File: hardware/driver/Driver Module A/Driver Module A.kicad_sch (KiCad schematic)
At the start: 22 parts, among them J1 Conn_01x02_Pin, J2 Conn_01x02_Pin, J3 Conn_01x01_Pin, J4 Conn_01x02_Pin

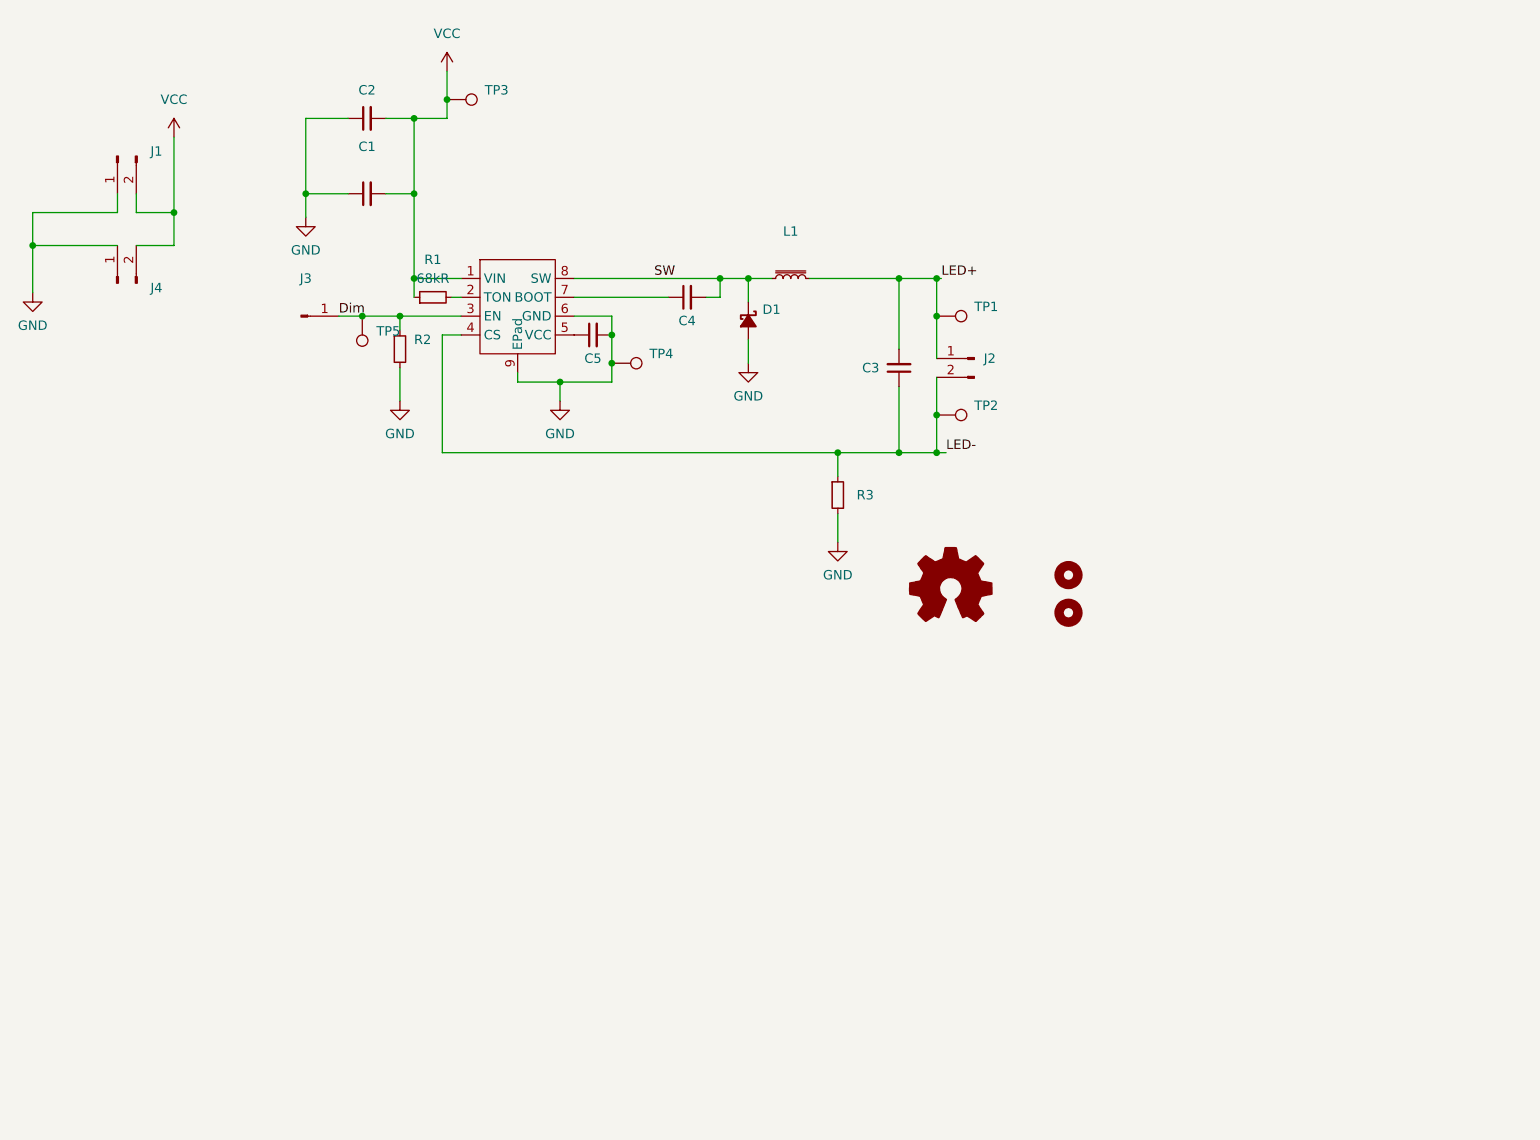
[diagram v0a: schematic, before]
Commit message: Minor silkscreen improvements on the driver module A
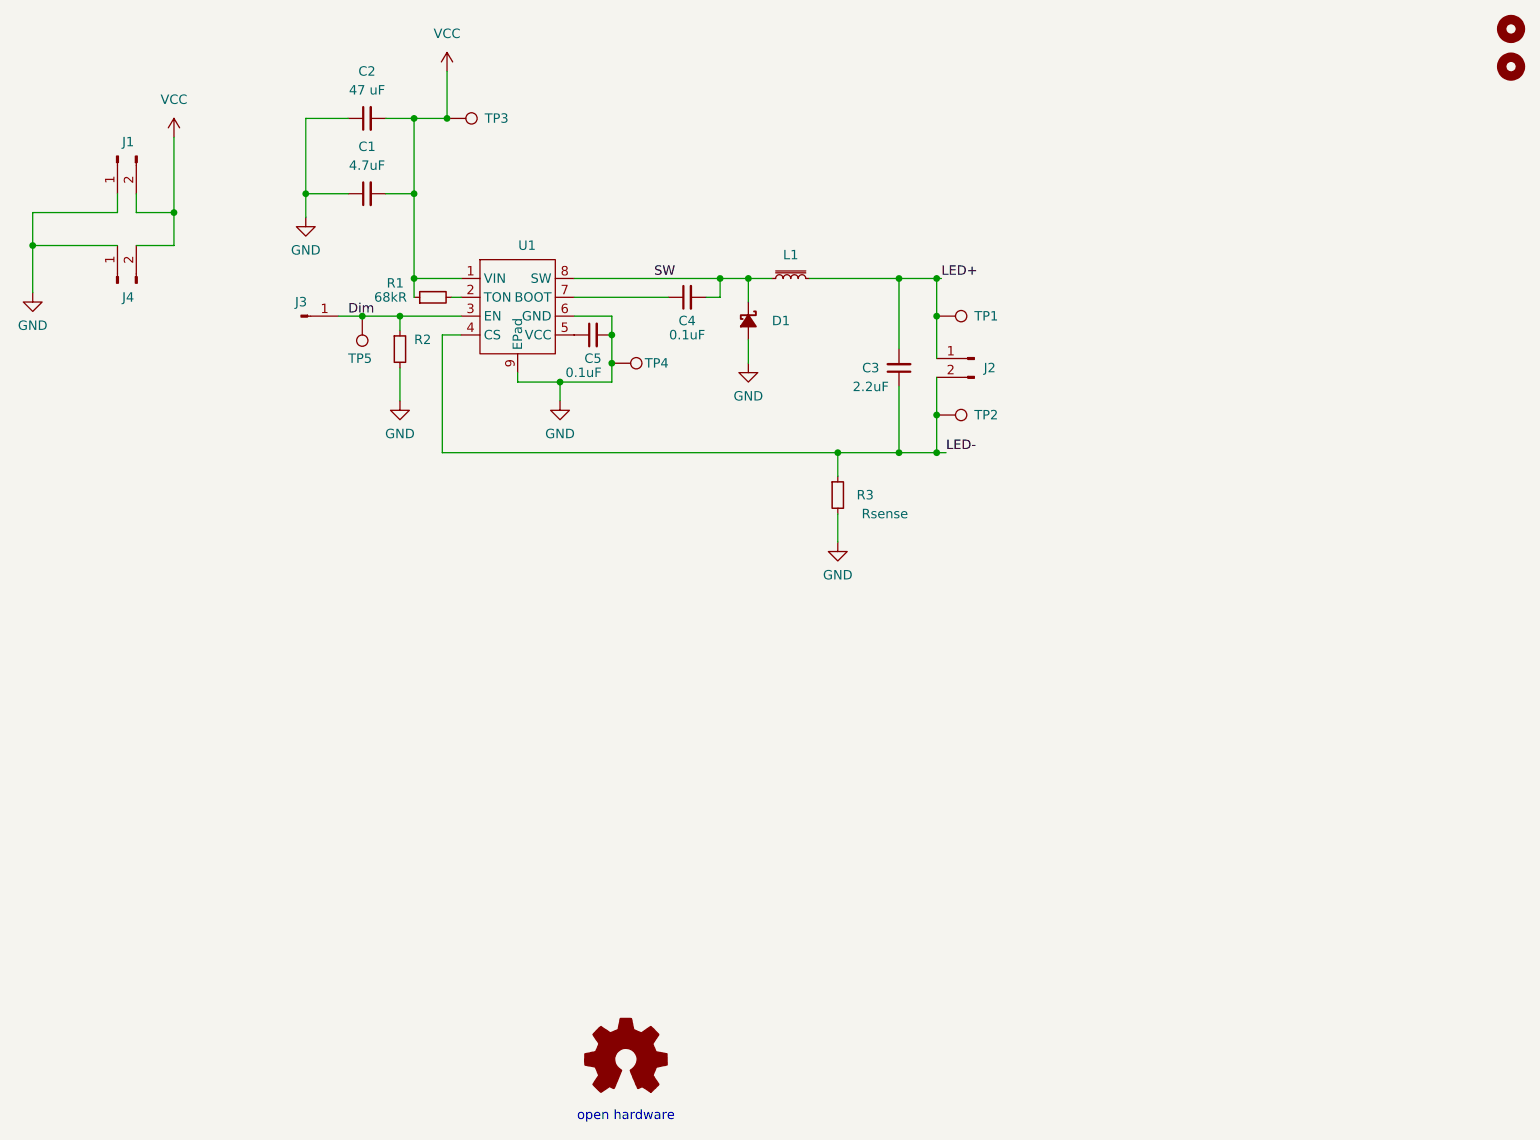
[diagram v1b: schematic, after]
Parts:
- C1: value C_Small -> 4.7uF
- C2: value C_Small -> 47 uF
- C4, C5: value C_Small -> 0.1uF
- R3: AltName (none) -> Rsense
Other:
- note added: "open hardware"
- moved on the sheet: TP3
